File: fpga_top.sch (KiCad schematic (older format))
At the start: 1 part, among them U8 10M16DCF256I7G_mk3pinstest

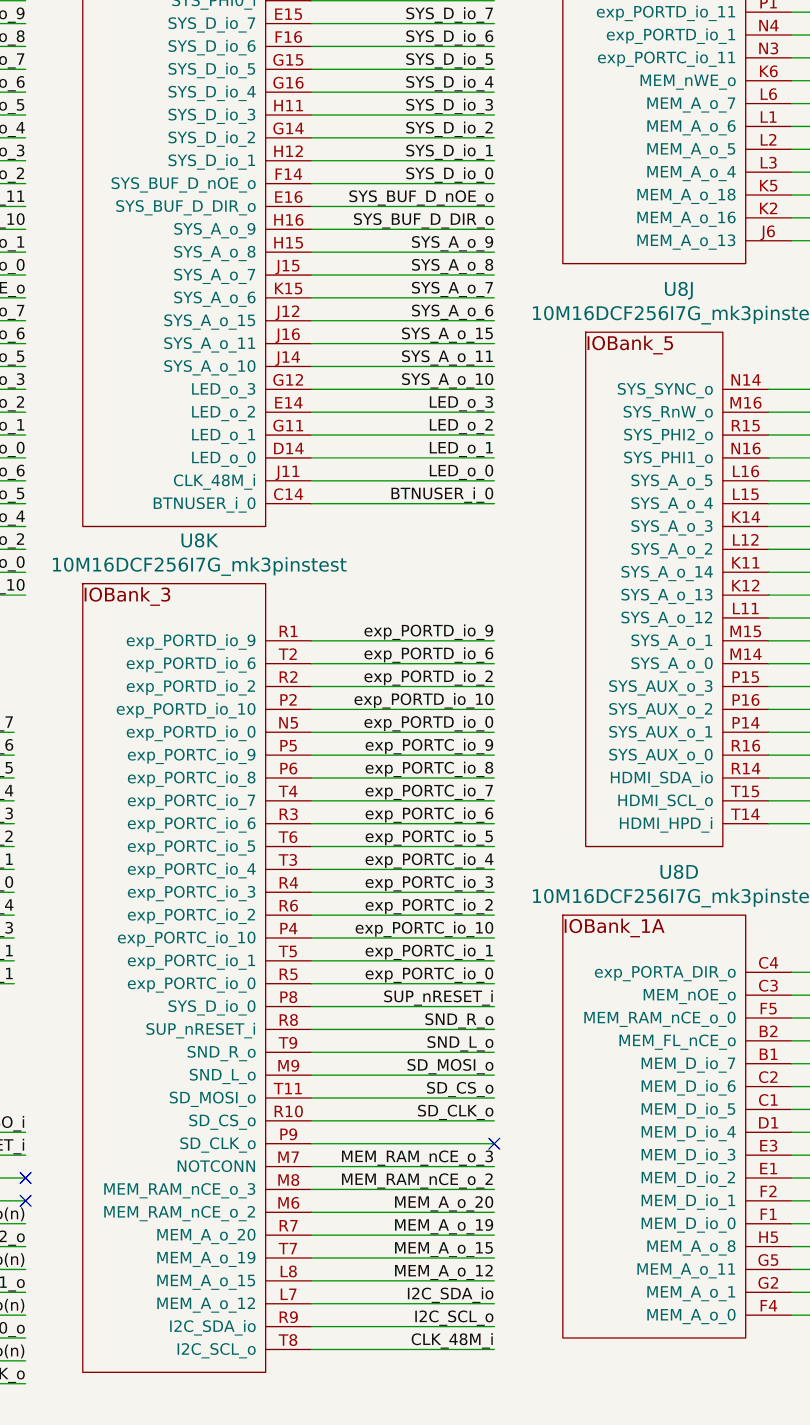
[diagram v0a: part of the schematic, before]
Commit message: Mk.3 fixes and new 68000 expansion board
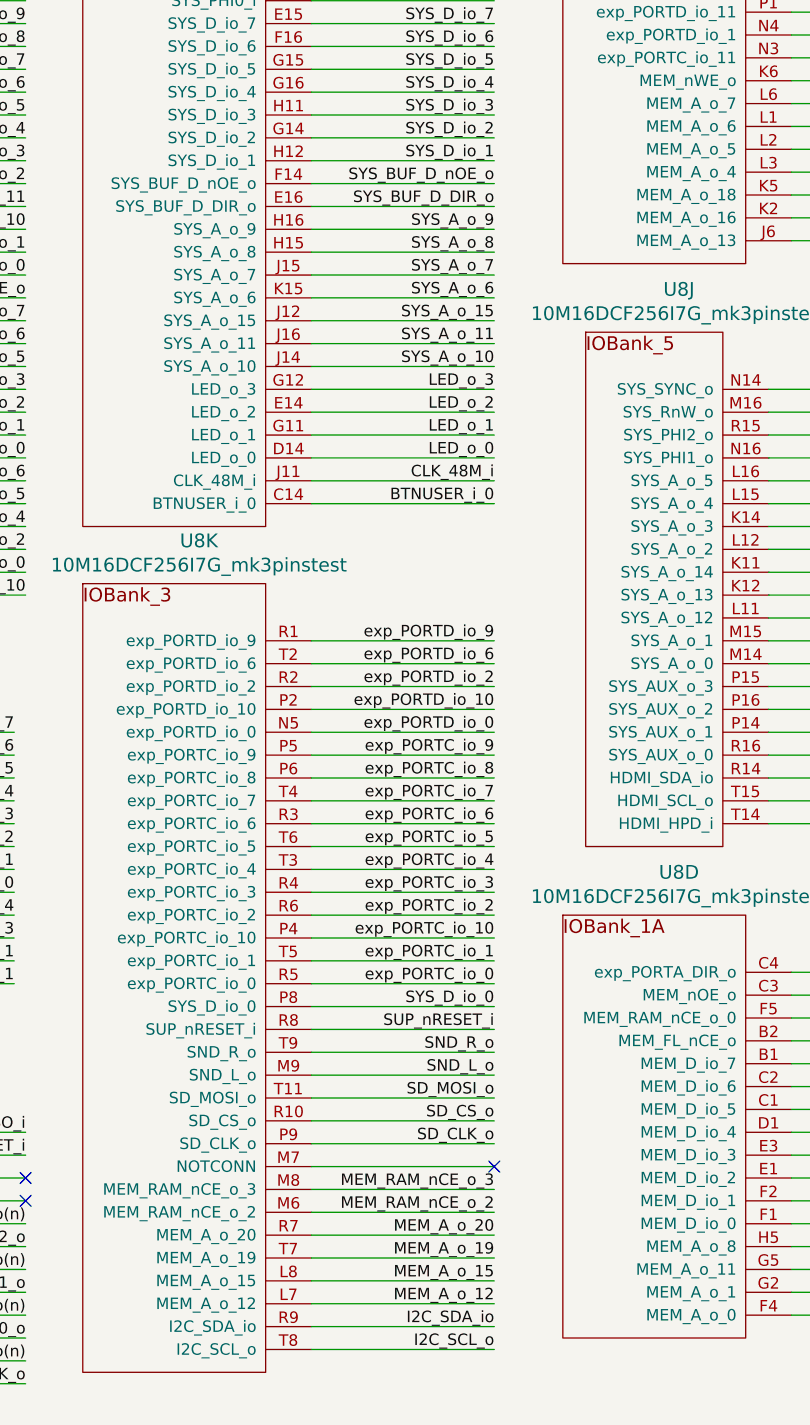
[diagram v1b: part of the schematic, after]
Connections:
- net CLK_48M: now also U8.J11 (CLK_48M_i); no longer U8.T8 (I2C_SCL_o)
- net I2C_SCL: now also U8.T8 (I2C_SCL_o); no longer U8.R9 (I2C_SDA_io)
- net I2C_SDA: now also U8.R9 (I2C_SDA_io); no longer U8.L7 (MEM_A_o_12)
- net LED_o_0: now also U8.D14 (LED_o_0); no longer U8.J11 (CLK_48M_i)
- net LED_o_1: now also U8.G11 (LED_o_1); no longer U8.D14 (LED_o_0)
- net LED_o_2: now also U8.E14 (LED_o_2); no longer U8.G11 (LED_o_1)
- net LED_o_3: now also U8.G12 (LED_o_3); no longer U8.E14 (LED_o_2)
- net MEM_A_o_12: now also U8.L7 (MEM_A_o_12); no longer U8.L8 (MEM_A_o_15)
- net MEM_A_o_15: now also U8.L8 (MEM_A_o_15); no longer U8.T7 (MEM_A_o_19)
- net MEM_A_o_19: now also U8.T7 (MEM_A_o_19); no longer U8.R7 (MEM_A_o_20)
- net MEM_A_o_20: now also U8.R7 (MEM_A_o_20); no longer U8.M6 (MEM_RAM_nCE_o_2)
- net MEM_RAM_nCE_o_2: now also U8.M6 (MEM_RAM_nCE_o_2); no longer U8.M8 (MEM_RAM_nCE_o_3)
- net MEM_RAM_nCE_o_3: now also U8.M8 (MEM_RAM_nCE_o_3); no longer U8.M7 (NOTCONN)
- net SD_CLK: now also U8.P9 (SD_CLK_o); no longer U8.R10 (SD_CS_o)
- net SD_CS: now also U8.R10 (SD_CS_o); no longer U8.T11 (SD_MOSI_o)
- net SD_MOSI: now also U8.T11 (SD_MOSI_o); no longer U8.M9 (SND_L_o)
- net SND_L: now also U8.M9 (SND_L_o); no longer U8.T9 (SND_R_o)
- net SND_R: now also U8.T9 (SND_R_o); no longer U8.R8 (SUP_nRESET_i)
- net SUP_nRES: now also U8.R8 (SUP_nRESET_i); no longer U8.P8 (SYS_D_io_0)
- net SYS_A_o_10: now also U8.J14 (SYS_A_o_10); no longer U8.G12 (LED_o_3)
- net SYS_A_o_11: now also U8.J16 (SYS_A_o_11); no longer U8.J14 (SYS_A_o_10)
- net SYS_A_o_15: now also U8.J12 (SYS_A_o_15); no longer U8.J16 (SYS_A_o_11)
- net SYS_A_o_6: now also U8.K15 (SYS_A_o_6); no longer U8.J12 (SYS_A_o_15)
- net SYS_A_o_7: now also U8.J15 (SYS_A_o_7); no longer U8.K15 (SYS_A_o_6)
- net SYS_A_o_8: now also U8.H15 (SYS_A_o_8); no longer U8.J15 (SYS_A_o_7)
- net SYS_A_o_9: now also U8.H16 (SYS_A_o_9); no longer U8.H15 (SYS_A_o_8)
- net SYS_BUFD_DIR: now also U8.E16 (SYS_BUF_D_DIR_o); no longer U8.H16 (SYS_A_o_9)
- net SYS_BUFD_nOE: now also U8.F14 (SYS_BUF_D_nOE_o); no longer U8.E16 (SYS_BUF_D_DIR_o)
- net SYS_D_io_0: now also U8.P8 (SYS_D_io_0); no longer U8.F14 (SYS_BUF_D_nOE_o)
